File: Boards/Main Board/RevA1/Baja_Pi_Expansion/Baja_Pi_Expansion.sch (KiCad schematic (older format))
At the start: 13 parts, among them J1 Conn_02x10_Counter_Clockwise, J2 Conn_02x12_Counter_Clockwise, J3 Screw_Terminal_01x04, J4 Conn_02x20_Odd_Even, J5 Conn_01x03_Male, J6 Screw_Terminal_01x07, U1 HDSP-7403

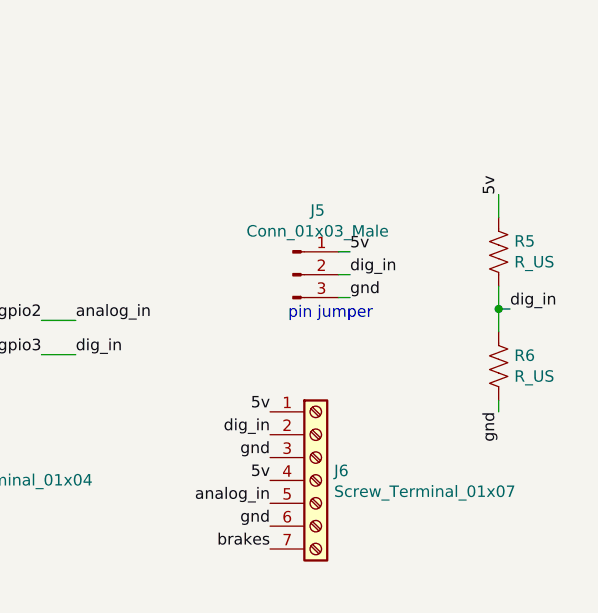
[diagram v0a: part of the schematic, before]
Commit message: Updated Pullup/Pulldown Jumper Mistake
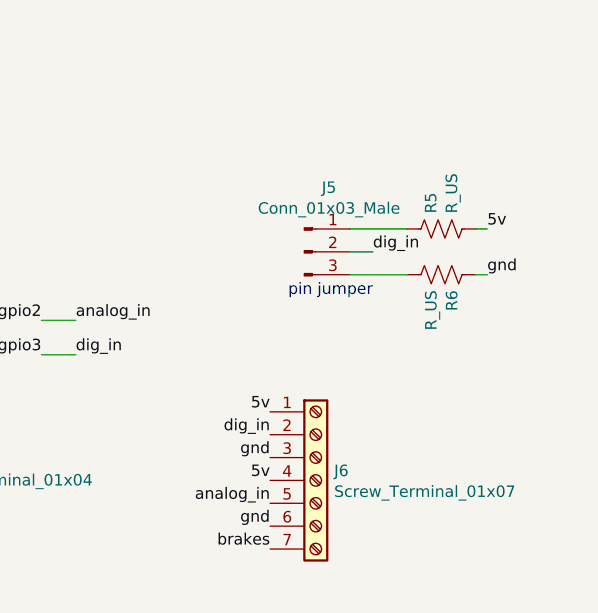
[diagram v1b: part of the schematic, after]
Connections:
- net 5v: now also R5.2; no longer J5.1 (Pin_1), R5.1
- net dig_in: no longer R5.2, R6.1
- net gnd: now also R6.1; no longer J5.3 (Pin_3), R6.2
- new net: J5.1 (Pin_1), R5.1
- new net: J5.3 (Pin_3), R6.2
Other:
- moved on the sheet: J5, R5, R6
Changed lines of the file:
@@
 L Connector:Conn_01x03_Male J5
 U 1 1 61637A7E
-P 9900 5200
-F 0 "J5" H 10008 5481 50  0000 C CNN
-F 1 "Conn_01x03_Male" H 10008 5390 50  0000 C CNN
-F 2 "Connector_PinHeader_2.54mm:PinHeader_1x03_P2.54mm_Vertical" H 9900 5200 50  0001 C CNN
-F 3 "~" H 9900 5200 50  0001 C CNN
-	1    9900 5200
+P 9950 5100
+F 0 "J5" H 10058 5381 50  0000 C CNN
+F 1 "Conn_01x03_Male" H 10058 5290 50  0000 C CNN
+F 2 "Connector_PinHeader_2.54mm:PinHeader_1x03_P2.54mm_Vertical" H 9950 5100 50  0001 C CNN
+F 3 "~" H 9950 5100 50  0001 C CNN
+	1    9950 5100
 	1    0    0    -1
 $EndComp
@@
 Text Label 9800 6000 2    50   ~ 0
 gnd
-Text Label 10150 5300 0    50   ~ 0
-gnd
-Text Label 10150 5200 0    50   ~ 0
+Text Label 10250 5100 0    50   ~ 0
 dig_in
-Text Label 10150 5100 0    50   ~ 0
-5v
 Text Label 9800 5800 2    50   ~ 0
 5v
@@
 analog_in
 $Comp
-L Device:R_US R5
-U 1 1 6163FA23
-P 10800 5100
-F 0 "R5" H 10868 5146 50  0000 L CNN
-F 1 "R_US" H 10868 5055 50  0000 L CNN
-F 2 "Resistor_SMD:R_0603_1608Metric" V 10840 5090 50  0001 C CNN
-F 3 "~" H 10800 5100 50  0001 C CNN
-	1    10800 5100
-	1    0    0    -1
-$EndComp
-$Comp
 L Device:R_US R6
 U 1 1 6163FA29
-P 10800 5600
-F 0 "R6" H 10868 5646 50  0000 L CNN
-F 1 "R_US" H 10868 5555 50  0000 L CNN
-F 2 "Resistor_SMD:R_0603_1608Metric" V 10840 5590 50  0001 C CNN
-F 3 "~" H 10800 5600 50  0001 C CNN
-	1    10800 5600
-	1    0    0    -1
+P 10550 5200
+F 0 "R6" H 10618 5246 50  0000 L CNN
+F 1 "R_US" H 10618 5155 50  0000 L CNN
+F 2 "Resistor_SMD:R_0603_1608Metric" V 10590 5190 50  0001 C CNN
+F 3 "~" H 10550 5200 50  0001 C CNN
+	1    10550 5200
+	0    1    1    0
 $EndComp
-Wire Wire Line
-	10800 5450 10800 5350
-Wire Wire Line
-	10850 5350 10800 5350
-Connection ~ 10800 5350
-Wire Wire Line
-	10800 5350 10800 5250
-Text Label 10850 5350 0    50   ~ 0
-dig_in
-Text Label 10800 4850 1    50   ~ 0
-5v
-Text Label 10800 5800 3    50   ~ 0
+Text Label 10750 5200 0    50   ~ 0
 gnd
 Text Label 8800 5400 2    50   ~ 0
@@
 Wire Wire Line
 	8950 5400 8800 5400
-Text Notes 10250 5400 2    50   ~ 0
+Text Notes 10250 5300 2    50   ~ 0
 pin jumper
 $Sheet
@@
 	5600 7050 5600 7000
 Wire Wire Line
-	10150 5100 10100 5100
-Wire Wire Line
-	10150 5200 10100 5200
-Wire Wire Line
-	10150 5300 10100 5300
-Wire Wire Line
-	10800 4950 10800 4850
-Wire Wire Line
-	10800 5800 10800 5750
+	10750 5200 10700 5200
 Wire Wire Line
 	7900 5900 7950 5900
@@
 Wire Wire Line
 	7950 6200 7900 6200
+$Comp
+L Device:R_US R5
+U 1 1 6163FA23
+P 10550 5000
+F 0 "R5" H 10618 5046 50  0000 L CNN
+F 1 "R_US" H 10618 4955 50  0000 L CNN
+F 2 "Resistor_SMD:R_0603_1608Metric" V 10590 4990 50  0001 C CNN
+F 3 "~" H 10550 5000 50  0001 C CNN
+	1    10550 5000
+	0    -1   -1   0
+$EndComp
+Text Label 10750 5000 0    50   ~ 0
+5v
+Wire Wire Line
+	10150 5000 10400 5000
+Wire Wire Line
+	10750 5000 10700 5000
+Wire Wire Line
+	10400 5200 10150 5200
+Wire Wire Line
+	10250 5100 10150 5100
 $EndSCHEMATC
